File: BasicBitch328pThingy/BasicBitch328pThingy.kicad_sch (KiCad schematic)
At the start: 26 parts, among them IC1 LM2597MX-5.0_NOPB, J3 Conn_02x03_Odd_Even, J4 Conn_01x08, J5 Conn_01x03, P1 Screw_Terminal_01x02, Q13 IRF9Z34NPBF, U1 ATmega328-P, U2 178.6165.0001, Y1 Crystal

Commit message: V1.0.1
* Fixed a trace issue
* updated Fab Files
* added bom/ibom.html
* added some code
** BasicFrameWork.ino
** Test.ino
** HeadLightWarningAndEGR.ino
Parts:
- C2: value 220nF -> 22pF

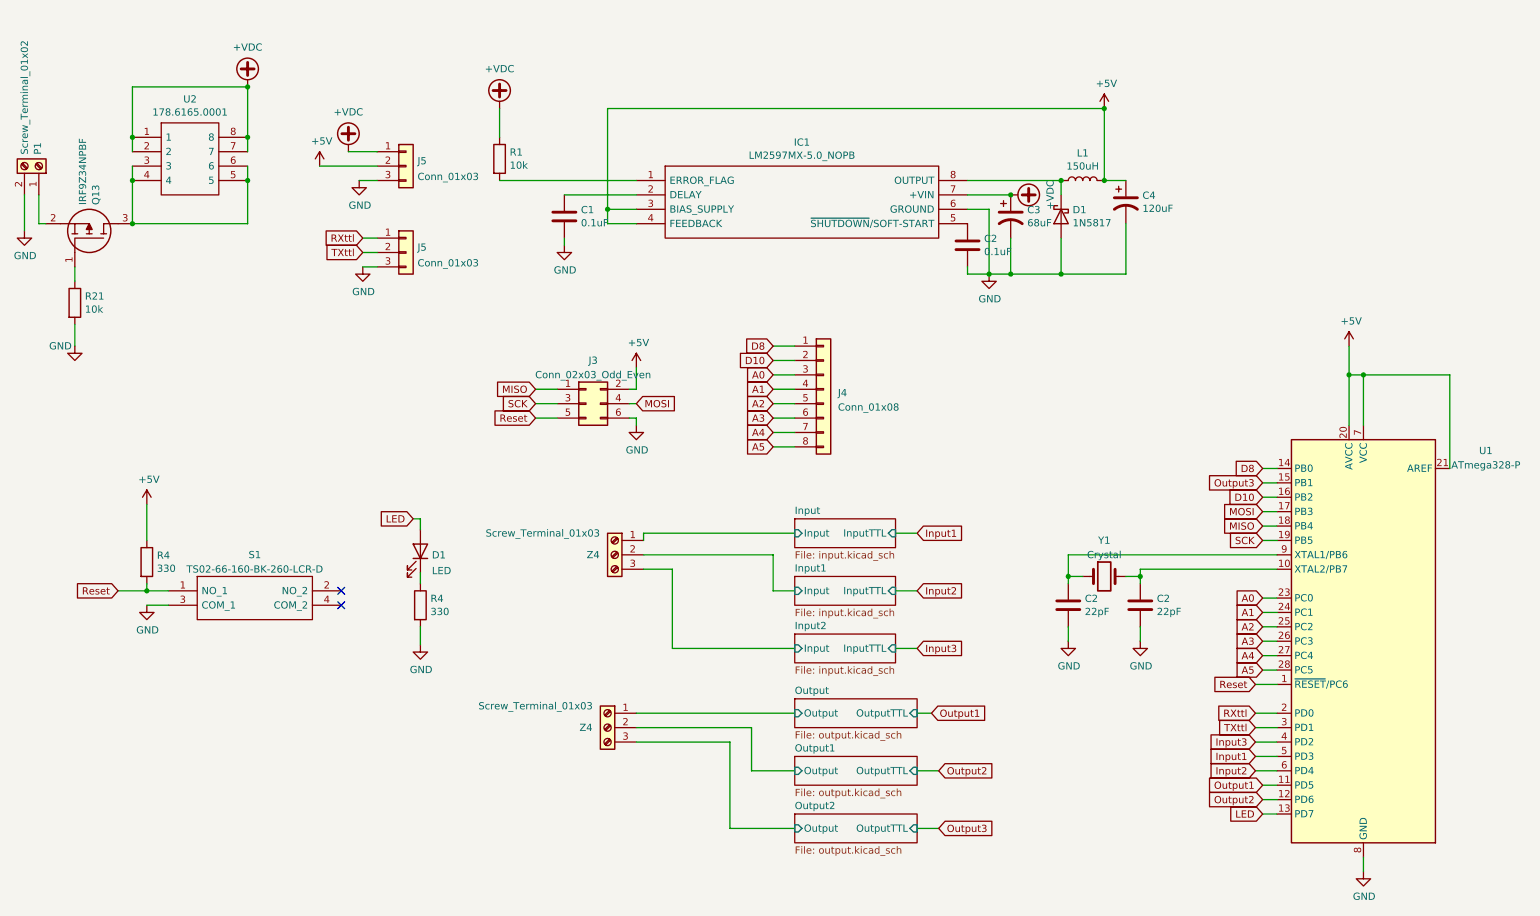
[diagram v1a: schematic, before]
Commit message: revamping this to have a CANBus Interface and swaping things to a SMD to save Space.
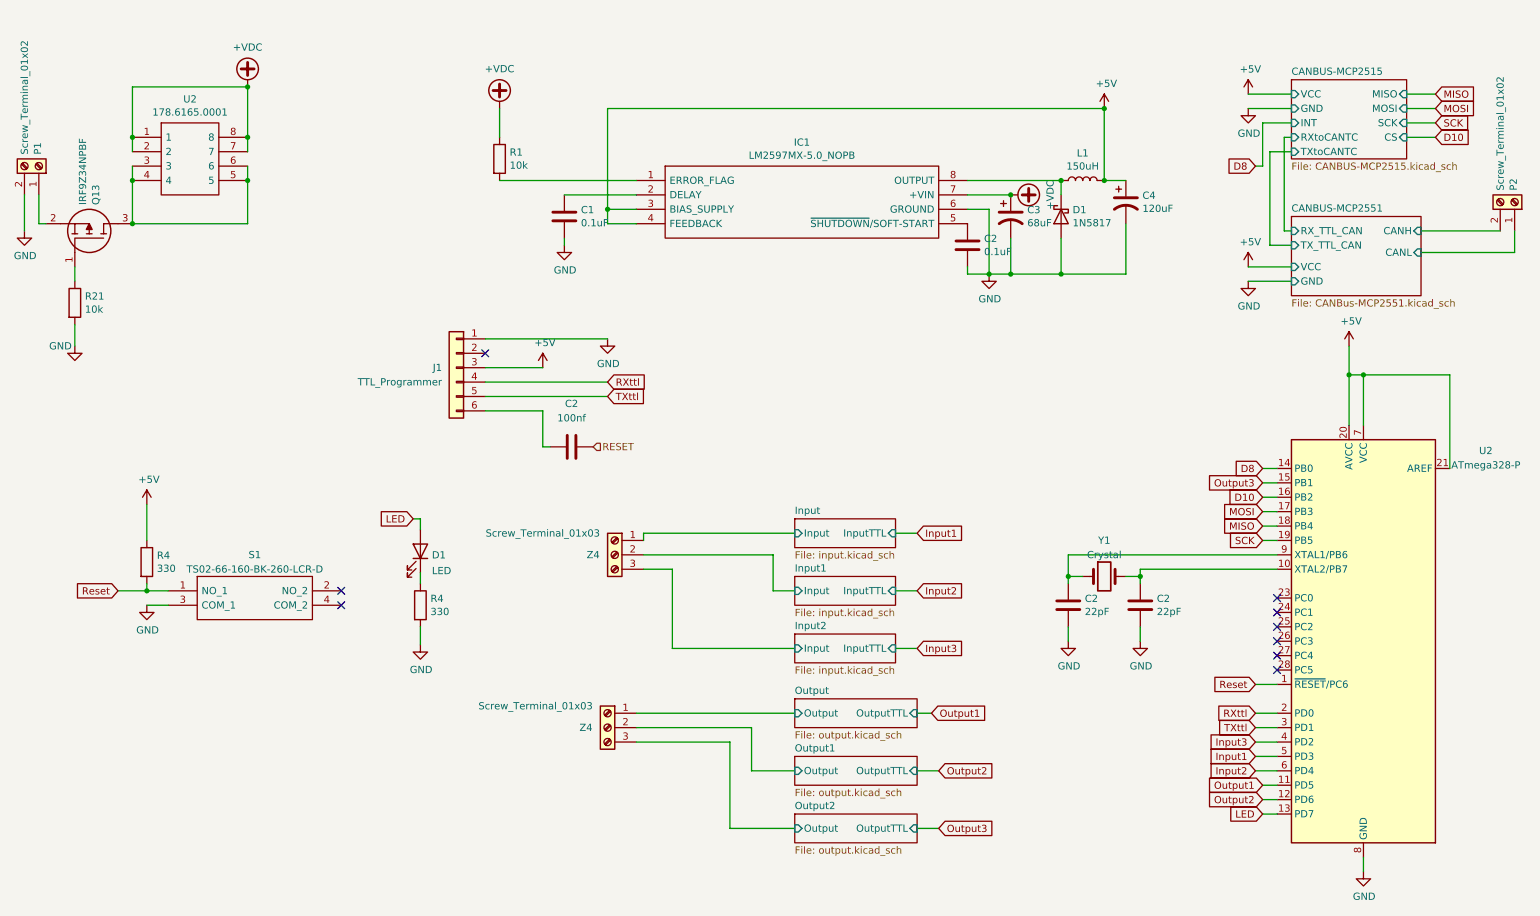
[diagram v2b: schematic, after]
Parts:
- removed J3: Conn_02x03_Odd_Even, Connector_PinHeader_2.54mm:PinHeader_2x03_P2.54mm_Vertical, symbol Connector_Generic:Conn_02x03_Odd_Even
- removed J4: Conn_01x08, Connector_PinHeader_2.54mm:PinHeader_1x08_P2.54mm_Vertical, symbol Connector_Generic:Conn_01x08
- removed J5 (x2): Conn_01x03, Connector_PinHeader_2.54mm:PinHeader_1x03_P2.54mm_Vertical, symbol Connector_Generic:Conn_01x03
- added C2: 100nf, Capacitor_SMD:C_1206_3216Metric_Pad1.33x1.80mm_HandSolder, symbol Device:C
- added J1: TTL_Programmer, Connector_PinHeader_2.54mm:PinHeader_1x06_P2.54mm_Vertical, symbol Connector_Generic:Conn_01x06
- added P2: Screw_Terminal_01x02, TerminalBlock_Phoenix:TerminalBlock_Phoenix_MKDS-1,5-2-5.08_1x02_P5.08mm_Horizontal, symbol Connector:Screw_Terminal_01x02
- C2: footprint Capacitor_THT:C_Disc_D5.1mm_W3.2mm_P5.00mm -> Capacitor_SMD:C_1206_3216Metric_Pad1.33x1.80mm_HandSolder
- R1: footprint Resistor_THT:R_Axial_DIN0207_L6.3mm_D2.5mm_P5.08mm_Vertical -> Resistor_SMD:R_1206_3216Metric_Pad1.30x1.75mm_HandSolder
- R21, R4: footprint Resistor_THT:R_Axial_DIN0207_L6.3mm_D2.5mm_P2.54mm_Vertical -> Resistor_SMD:R_1206_3216Metric_Pad1.30x1.75mm_HandSolder
- renumbered U1 to U2
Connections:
- net +5V: now also J1.3 (Pin_3)
- net GND: now also J1.1 (Pin_1)
- net RXttl: now also J1.4 (Pin_4)
- net TXttl: now also J1.5 (Pin_5)
- net A0: no longer names the net of U2.23 (PC0)
- net A1: no longer names the net of U2.24 (PC1)
- net A2: no longer names the net of U2.25 (PC2)
- net A3: no longer names the net of U2.26 (PC3)
- net A4: no longer names the net of U2.27 (PC4)
- net A5: no longer names the net of U2.28 (PC5)
- new net: C2.1, J1.6 (Pin_6)
- new net CANBUS-MCP2551/CANH: P2.2 (Pin_2)
- new net CANBUS-MCP2551/CANL: P2.1 (Pin_1)
- new net RESET: C2.2
- no-connect marks 2 -> 9
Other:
- added sheet CANBUS-MCP2515 (CANBUS-MCP2515.kicad_sch)
- added sheet CANBUS-MCP2551 (CANBus-MCP2551.kicad_sch)
